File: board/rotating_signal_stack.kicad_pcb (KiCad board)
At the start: 2 copper layers, 85 x 67 mm, 24 parts, among them J1 RJ45_LED_Shielded, J3 Motor pins, J4 Molex_Megafit_02, Q1 TPC8132_LQS, SW1 SW_Push, SW2 SW_Push

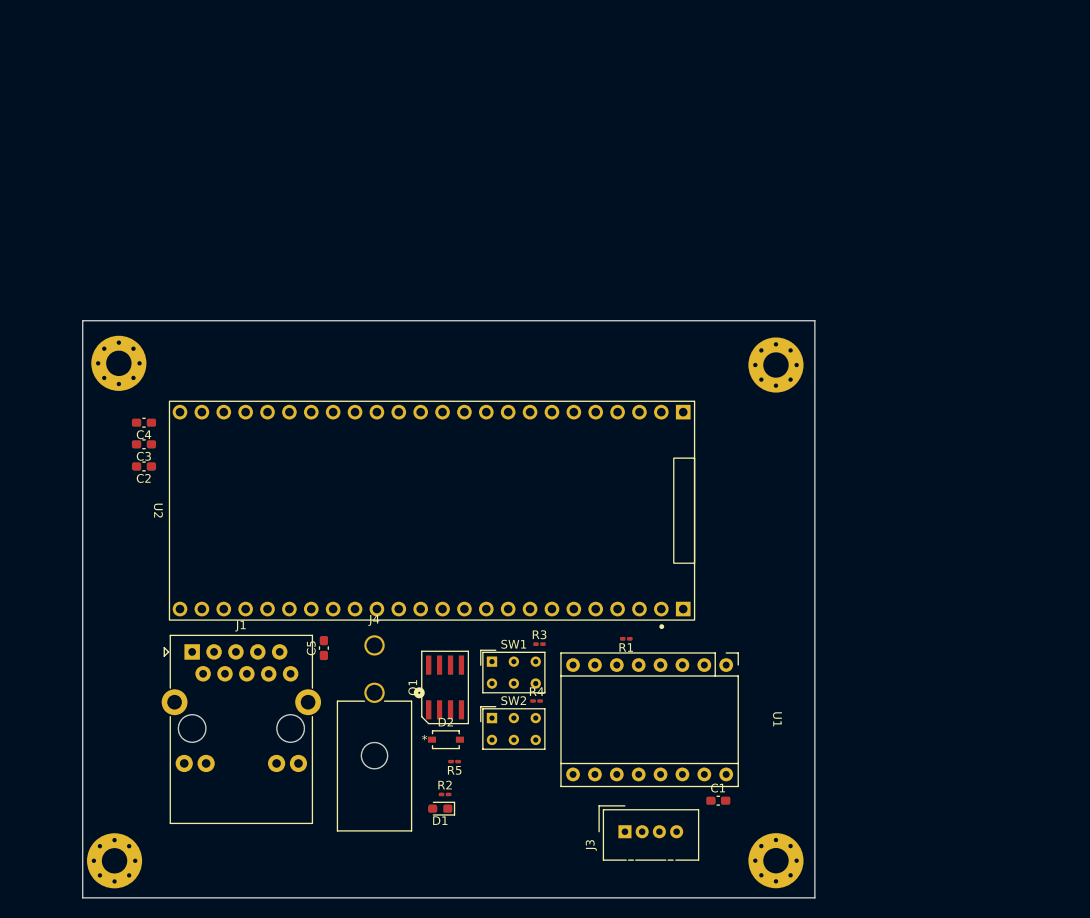
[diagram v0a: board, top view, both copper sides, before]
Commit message: Made some progress in the footprint.
I need to change the STM32CubeMX pin locations to make the footprint less messy, but I will work on this more sometime next week.
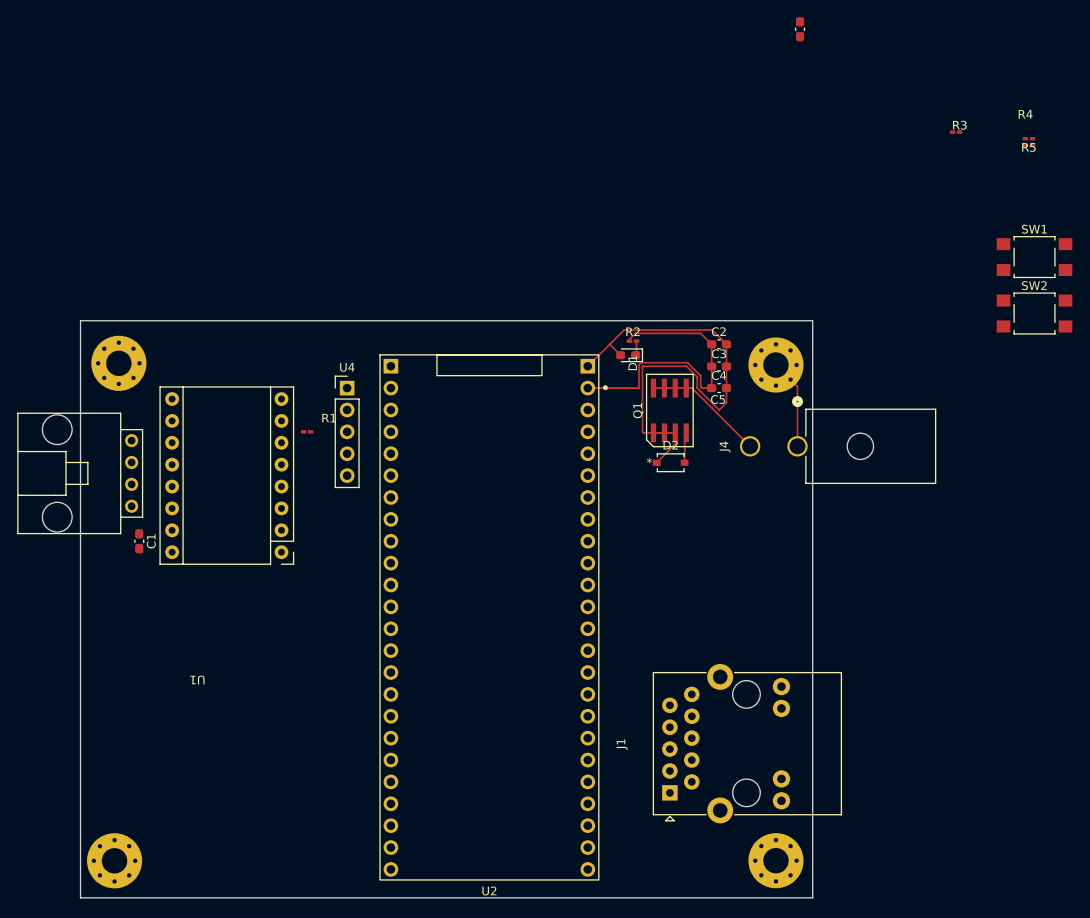
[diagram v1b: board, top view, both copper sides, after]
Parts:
- added U4: ~, Connector_PinHeader_2.54mm:PinHeader_1x05_P2.54mm_Vertical, F.Cu at (139.7, 83.8)
- C3: value 0.1 uF -> 10 uF
- J3: footprint Connector:NS-Tech_Grove_1x04_P2mm_Vertical -> MRDT_Connectors:MOLEX_SL_04_Horizontal
- SW1, SW2: footprint Button_Switch_THT:SW_NKK_GW12LJP -> MRDT_Switches:SW_SPST_TL3305A
- moved R5 98.4 mm to (218.8, 54.9)
- moved C5 90.6 mm to (192.3, 42.2), turned to -90 degrees
- moved R4 86.2 mm to (218.8, 55.6)
- moved SW1 78.6 mm to (219.5, 68.6)
- moved SW2 78.6 mm to (219.5, 75.2)
- moved R3 76.6 mm to (210.4, 54.1)
- moved C1 73.7 mm to (115.6, 101.6), turned to -90 degrees
- moved J3 68.6 mm to (114.7, 97.5)
- moved C2 68.3 mm to (182.9, 78.7), turned to 0 degrees
- moved C3 67.4 mm to (182.9, 81.3), turned to 0 degrees
- moved C4 66.9 mm to (182.9, 83.8), turned to 0 degrees
- moved U1 64.9 mm to (125.8, 108.3), turned to 180 degrees
- moved J1 57.8 mm to (177.2, 130.8), turned to 90 degrees
- moved R2 57.0 mm to (172.9, 78.4)
- moved D1 57.0 mm to (172.3, 80.0)
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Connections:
- U1 pad 11: Net-(J3-Pin_4) -> Net-(J3-Pin_1)
- U1 pad 12: Net-(J3-Pin_3) -> Net-(J3-Pin_2)
- U1 pad 13: Net-(J3-Pin_2) -> Net-(J3-Pin_3)
- U1 pad 14: Net-(J3-Pin_1) -> Net-(J3-Pin_4)
- U1 pad 2: M2 -> M0
- U1 pad 4: M0 -> M2
- U2 pad 10: DIR -> unconnected-(U2-PA10-Pad10)
- U2 pad 12: INT -> unconnected-(U2-PA8-Pad12)
- U2 pad 18: nSTBY -> unconnected-(U2-PB13-Pad18)
- U2 pad 27: unconnected-(U2-PB5-Pad27) -> nSTBY
- U2 pad 28: unconnected-(U2-PB6-Pad28) -> DIR
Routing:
- net +12V: track 0.00 -> 55.9 mm
- net GND: track 0.00 -> 42.8 mm
- net Net-(J4-Pad2): track 0.00 -> 14.0 mm
- net Net-(D2-Pad2): track 0.00 -> 3.54 mm
- net Net-(D1-K): track 0.00 -> 1.68 mm
